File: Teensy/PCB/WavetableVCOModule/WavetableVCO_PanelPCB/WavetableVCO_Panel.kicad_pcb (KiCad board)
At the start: 2 copper layers, 61 x 128 mm, 15 parts, among them SW1 Next_File_Button

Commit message: Generated Gerbers
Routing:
- added copper zone on B.Cu, net extra
- added copper zone on F.Cu, net extra
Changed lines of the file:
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@@
       (layerselection 0x00010fc_ffffffff)
       (disableapertmacros false)
-      (usegerberextensions false)
-      (usegerberattributes true)
-      (usegerberadvancedattributes true)
-      (creategerberjobfile true)
+      (usegerberextensions true)
+      (usegerberattributes false)
+      (usegerberadvancedattributes false)
+      (creategerberjobfile false)
       (svguseinch false)
       (svgprecision 6)
@@
       (psa4output false)
       (plotreference true)
-      (plotvalue true)
+      (plotvalue false)
       (plotinvisibletext false)
       (sketchpadsonfab false)
-      (subtractmaskfromsilk false)
+      (subtractmaskfromsilk true)
       (outputformat 1)
       (mirror false)
-      (drillshape 1)
+      (drillshape 0)
       (scaleselection 1)
-      (outputdirectory "")
+      (outputdirectory "WavetableVCO_Panel_Gerber/")
     )
   )
   (net 0 "")
+  (net 1 "extra")
   (footprint "Perfboard:3.5mm Jack Perfboard_Hole" (layer "F.Cu")
     (at 129.54 154.1)
@@
       (effects (font (size 1 1) (thickness 0.15)))
     )
+    (fp_line (start -2.54 -64) (end 2.54 -64) (layer "User.1") (width 0.12))
     (fp_line (start -2.54 64) (end 2.54 64) (layer "User.1") (width 0.12))
-    (fp_line (start -2.54 -64) (end 2.54 -64) (layer "User.1") (width 0.12))
     (fp_circle (center 0 0) (end 0 0) (layer "User.1") (width 0.12) (fill none))
-    (fp_line (start -1.27 59.65) (end 1.27 59.65) (layer "User.2") (width 0.12))
-    (fp_line (start -1.27 62.85) (end 1.27 62.85) (layer "User.2") (width 0.12))
-    (fp_line (start -1.27 -62.85) (end 1.27 -62.85) (layer "User.2") (width 0.12))
-    (fp_line (start -1.27 -59.65) (end 1.27 -59.65) (layer "User.2") (width 0.12))
-    (fp_arc (start -1.27 62.85) (mid -2.87 61.25) (end -1.27 59.65) (layer "User.2") (width 0.12))
-    (fp_arc (start 1.27 59.65) (mid 2.87 61.25) (end 1.27 62.85) (layer "User.2") (width 0.12))
-    (fp_arc (start -1.27 -59.65) (mid -2.87 -61.25) (end -1.27 -62.85) (layer "User.2") (width 0.12))
-    (fp_arc (start 1.27 -62.85) (mid 2.87 -61.25) (end 1.27 -59.65) (layer "User.2") (width 0.12))
-    (pad "" np_thru_hole oval (at 0 -61.25) (size 5.74 3.2) (drill oval 5.74 3.2) (layers *.Mask))
-    (pad "" np_thru_hole oval (at 0 61.25) (size 5.74 3.2) (drill oval 5.74 3.2) (layers *.Mask))
+    (fp_line (start -1.6 59.65) (end 1.6 59.65) (layer "User.2") (width 0.12))
+    (fp_line (start -1.6 -59.65) (end 1.6 -59.65) (layer "User.2") (width 0.12))
+    (fp_line (start -1.6 62.85) (end 1.6 62.85) (layer "User.2") (width 0.12))
+    (fp_line (start -1.6 -62.85) (end 1.6 -62.85) (layer "User.2") (width 0.12))
+    (fp_arc (start 1.6 59.65) (mid 3.2 61.25) (end 1.6 62.85) (layer "User.2") (width 0.12))
+    (fp_arc (start 1.6 -62.85) (mid 3.2 -61.25) (end 1.6 -59.65) (layer "User.2") (width 0.12))
+    (fp_arc (start -1.6 -59.65) (mid -3.2 -61.25) (end -1.6 -62.85) (layer "User.2") (width 0.12))
+    (fp_arc (start -1.6 62.85) (mid -3.2 61.25) (end -1.6 59.65) (layer "User.2") (width 0.12))
+    (pad "1" thru_hole oval (at 0 -61.25) (size 7.4 4.2) (drill oval 6.4 3.2) (layers *.Cu *.Mask)
+      (net 1 "extra"))
+    (pad "1" thru_hole oval (at 0 61.25) (size 7.4 4.2) (drill oval 6.4 3.2) (layers *.Cu *.Mask)
+      (net 1 "extra"))
   )
   (footprint "Potentiometer:Bourns_PTV09A-XF_Hole" (layer "F.Cu")
@@
     (fp_line (start -2.54 -64) (end 2.54 -64) (layer "User.1") (width 0.12))
     (fp_circle (center 0 0) (end 0 0) (layer "User.1") (width 0.12) (fill none))
-    (fp_line (start -1.27 -59.65) (end 1.27 -59.65) (layer "User.2") (width 0.12))
-    (fp_line (start -1.27 62.85) (end 1.27 62.85) (layer "User.2") (width 0.12))
-    (fp_line (start -1.27 59.65) (end 1.27 59.65) (layer "User.2") (width 0.12))
-    (fp_line (start -1.27 -62.85) (end 1.27 -62.85) (layer "User.2") (width 0.12))
-    (fp_arc (start -1.27 -59.65) (mid -2.87 -61.25) (end -1.27 -62.85) (layer "User.2") (width 0.12))
-    (fp_arc (start -1.27 62.85) (mid -2.87 61.25) (end -1.27 59.65) (layer "User.2") (width 0.12))
-    (fp_arc (start 1.27 -62.85) (mid 2.87 -61.25) (end 1.27 -59.65) (layer "User.2") (width 0.12))
-    (fp_arc (start 1.27 59.65) (mid 2.87 61.25) (end 1.27 62.85) (layer "User.2") (width 0.12))
-    (pad "" np_thru_hole oval (at 0 61.25) (size 5.74 3.2) (drill oval 5.74 3.2) (layers *.Mask))
-    (pad "" np_thru_hole oval (at 0 -61.25) (size 5.74 3.2) (drill oval 5.74 3.2) (layers *.Mask))
+    (fp_line (start -1.6 62.85) (end 1.6 62.85) (layer "User.2") (width 0.12))
+    (fp_line (start -1.6 -62.85) (end 1.6 -62.85) (layer "User.2") (width 0.12))
+    (fp_line (start -1.6 59.65) (end 1.6 59.65) (layer "User.2") (width 0.12))
+    (fp_line (start -1.6 -59.65) (end 1.6 -59.65) (layer "User.2") (width 0.12))
+    (fp_arc (start -1.6 62.85) (mid -3.2 61.25) (end -1.6 59.65) (layer "User.2") (width 0.12))
+    (fp_arc (start 1.6 59.65) (mid 3.2 61.25) (end 1.6 62.85) (layer "User.2") (width 0.12))
+    (fp_arc (start -1.6 -59.65) (mid -3.2 -61.25) (end -1.6 -62.85) (layer "User.2") (width 0.12))
+    (fp_arc (start 1.6 -62.85) (mid 3.2 -61.25) (end 1.6 -59.65) (layer "User.2") (width 0.12))
+    (pad "1" thru_hole oval (at 0 61.25) (size 7.4 4.2) (drill oval 6.4 3.2) (layers *.Cu *.Mask)
+      (net 1 "extra"))
+    (pad "1" thru_hole oval (at 0 -61.25) (size 7.4 4.2) (drill oval 6.4 3.2) (layers *.Cu *.Mask)
+      (net 1 "extra"))
   )
   (footprint "Perfboard:3.5mm Jack Perfboard_Hole" (layer "F.Cu")
@@
   (gr_rect (start 91.442322 56.66449) (end 126.999967 82.065685) (layer "Edge.Cuts") (width 0.05) (fill none))
   (gr_rect (start 78.74 45.72) (end 139.7 173.72) (layer "Edge.Cuts") (width 0.05) (fill none))
+  (zone (net 1) (net_name "extra") (layers F&B.Cu) (hatch edge 0.508)
+    (connect_pads yes (clearance 0.508))
+    (min_thickness 0.254) (filled_areas_thickness no)
+    (fill yes (thermal_gap 0.508) (thermal_bridge_width 0.508))
+    (polygon
+      (pts
+        (xy 139.7 173.736)
+        (xy 78.74 173.736)
+        (xy 78.74 45.72)
+        (xy 139.7 45.72)
+      )
+    )
+  )
 )

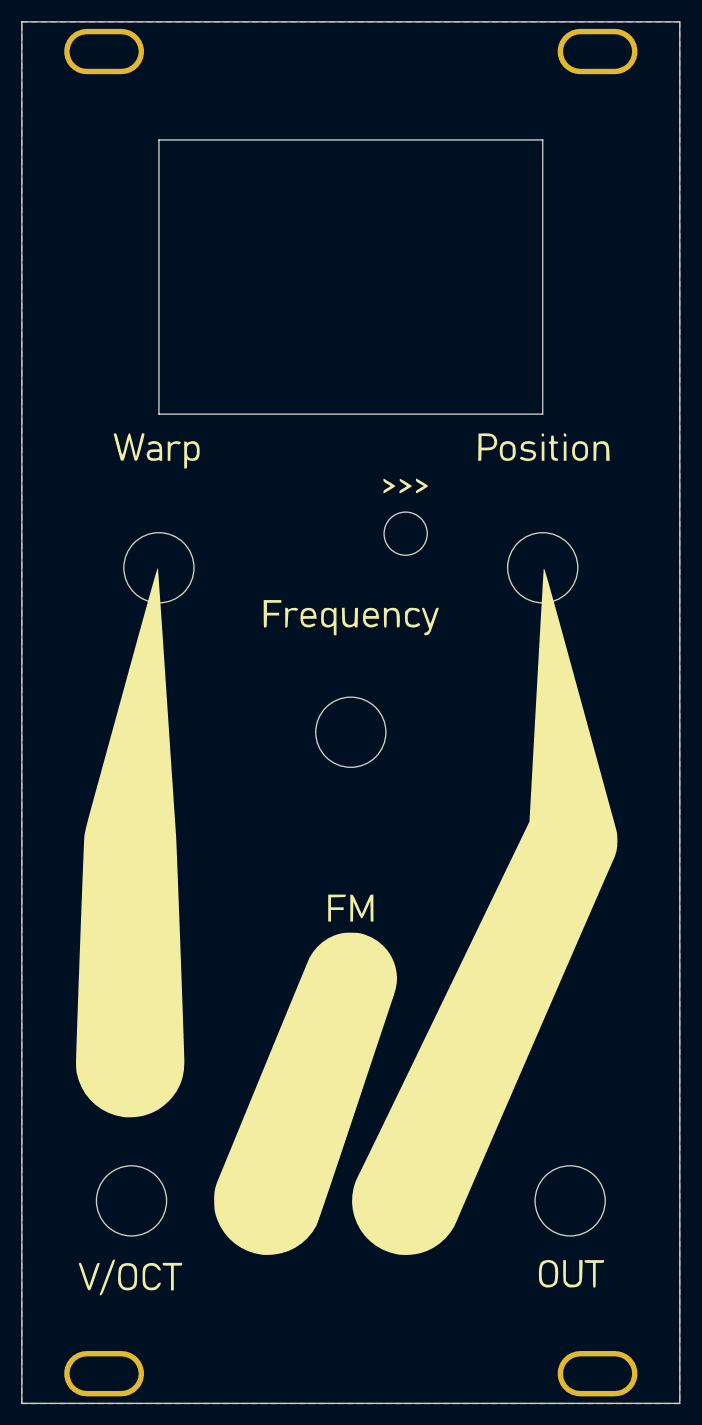
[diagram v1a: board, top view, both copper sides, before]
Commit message: Added USB-C Power Supply
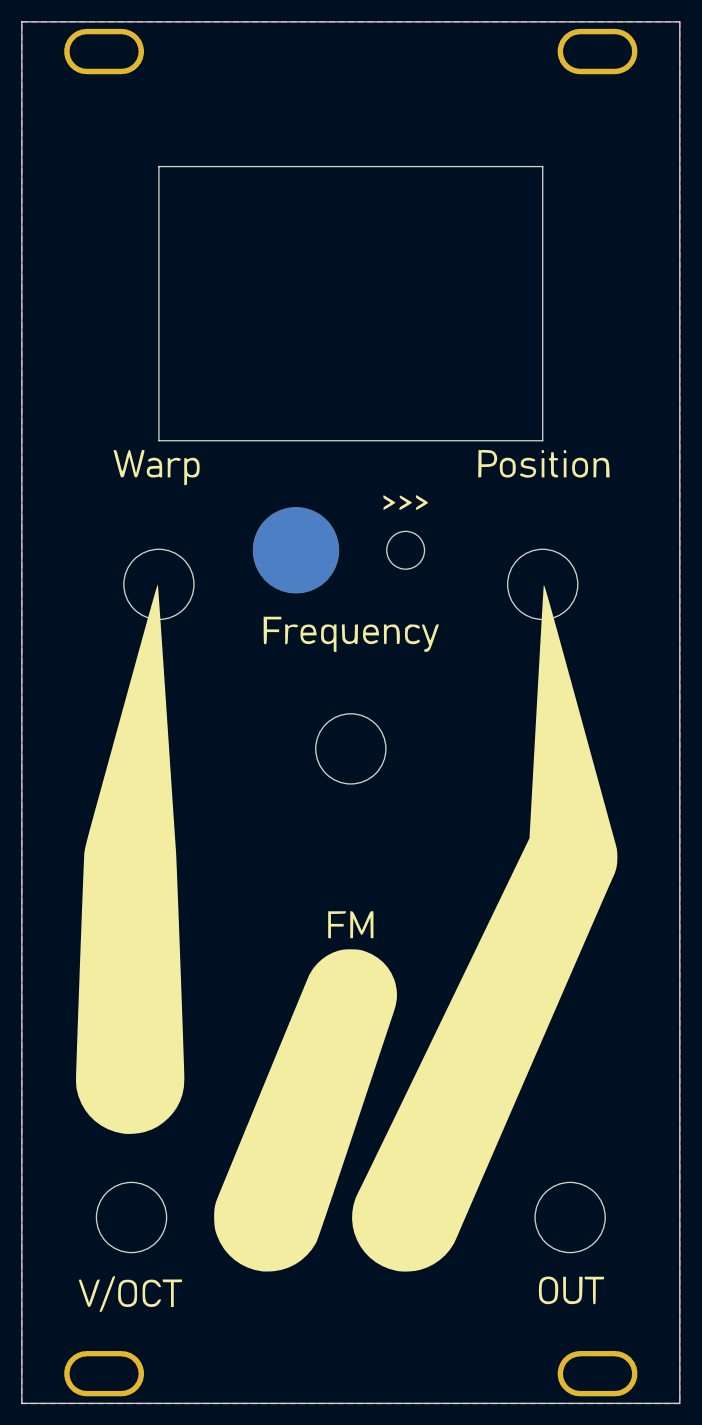
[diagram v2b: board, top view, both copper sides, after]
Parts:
- added REF**: Würth_REDCUBE_SMD_7466203, Misc:Würth_REDCUBE_SMD_7466203, B.Cu at (104.1, 94.7)
- moved G*** 1.54 mm to (109.2, 112.3)
- moved RV1 1.54 mm to (91.4, 104.8)
- moved RV5 1.54 mm to (127.0, 104.8)
- moved SW1 1.54 mm to (111.0, 92.4)
- moved IJ1 1.54 mm to (88.9, 142.9)
- moved IJ2 1.54 mm to (88.9, 155.6)
- moved IJ3 1.54 mm to (101.6, 155.6)
- moved IJ4 1.54 mm to (114.3, 155.6)
- moved OJ1 1.54 mm to (129.5, 155.6)
- moved RV2 1.54 mm to (88.8, 130.2)
- moved RV3 1.54 mm to (109.2, 120.1)
- moved RV4 1.54 mm to (109.2, 142.9)
- moved RV6 1.54 mm to (129.5, 130.2)
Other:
- outline, holes or cut-outs redrawn
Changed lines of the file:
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@@
   )
   (setup
+    (stackup
+      (layer "F.SilkS" (type "Top Silk Screen") (color "White"))
+      (layer "F.Paste" (type "Top Solder Paste"))
+      (layer "F.Mask" (type "Top Solder Mask") (color "Black") (thickness 0.01))
+      (layer "F.Cu" (type "copper") (thickness 0.035))
+      (layer "dielectric 1" (type "core") (thickness 1.51) (material "FR4") (epsilon_r 4.5) (loss_tangent 0.02))
+      (layer "B.Cu" (type "copper") (thickness 0.035))
+      (layer "B.Mask" (type "Bottom Solder Mask") (color "Black") (thickness 0.01))
+      (layer "B.Paste" (type "Bottom Solder Paste"))
+      (layer "B.SilkS" (type "Bottom Silk Screen") (color "White"))
+      (copper_finish "ENIG")
+      (dielectric_constraints no)
+    )
     (pad_to_mask_clearance 0)
     (pcbplotparams
@@
   (net 1 "extra")
   (footprint "Perfboard:3.5mm Jack Perfboard_Hole" (layer "F.Cu")
-    (at 129.54 154.1)
+    (at 129.54 155.64)
     (property "Sheetfile" "../Subcircuits/Output/Output.kicad_sch")
     (property "Sheetname" "Channel_1_Mod_Output")
@@
       (effects (font (size 1 1) (thickness 0.15)))
     )
-    (fp_text value "Screw_Slots" (at 0 5.08 unlocked) (layer "F.Fab")
-      (effects (font (size 1 1) (thickness 0.15)))
-    )
-    (fp_text user "${REFERENCE}" (at 0 6.58 unlocked) (layer "F.Fab")
+    (fp_text value "Screw_Slots" (at 0 6.62 unlocked) (layer "F.Fab")
+      (effects (font (size 1 1) (thickness 0.15)))
+    )
+    (fp_text user "${REFERENCE}" (at 0 8.12 unlocked) (layer "F.Fab")
       (effects (font (size 1 1) (thickness 0.15)))
     )
@@
   )
   (footprint "Potentiometer:Bourns_PTV09A-XF_Hole" (layer "F.Cu")
-    (at 91.44 103.3)
+    (at 91.44 104.84)
     (descr "Bourns_PTV09A-4025FB103, http://www.bourns.com/docs/Product-Datasheets/ptv09.pdf")
     (tags "Potentiometer vertical Bourns PTV09A-1 Single")
@@
       (effects (font (size 1 1) (thickness 0.15)))
     )
-    (fp_text user "${REFERENCE}" (at 0 -1.985 -180) (layer "F.Fab")
+    (fp_text user "${REFERENCE}" (at 0 -1.985) (layer "F.Fab")
       (effects (font (size 1 1) (thickness 0.15)))
     )
@@
   )
   (footprint "Potentiometer:Bourns_PTV09A-X_Hole" (layer "F.Cu")
-    (at 109.22 141.4)
+    (at 109.22 142.94)
     (descr "Bourns_PTV09A-4025FB103, http://www.bourns.com/docs/Product-Datasheets/ptv09.pdf")
     (tags "Potentiometer vertical Bourns PTV09A-1 Single")
@@
       (effects (font (size 1 1) (thickness 0.15)))
     )
-    (fp_text user "${REFERENCE}" (at 0 -1.985 -180) (layer "F.Fab")
+    (fp_text user "${REFERENCE}" (at 0 -1.985) (layer "F.Fab")
       (effects (font (size 1 1) (thickness 0.15)))
     )
@@
   )
   (footprint "Potentiometer:Bourns_PTV09A-X_Hole" (layer "F.Cu")
-    (at 129.495 128.685)
+    (at 129.495 130.225)
     (descr "Bourns_PTV09A-4025FB103, http://www.bourns.com/docs/Product-Datasheets/ptv09.pdf")
     (tags "Potentiometer vertical Bourns PTV09A-1 Single")
@@
       (effects (font (size 1 1) (thickness 0.15)))
     )
-    (fp_text user "${REFERENCE}" (at 0 -1.985 -180) (layer "F.Fab")
+    (fp_text user "${REFERENCE}" (at 0 -1.985) (layer "F.Fab")
       (effects (font (size 1 1) (thickness 0.15)))
     )
@@
       (effects (font (size 1 1) (thickness 0.15)))
     )
-    (fp_text value "Screw_Slots" (at 0 5.08 unlocked) (layer "F.Fab")
-      (effects (font (size 1 1) (thickness 0.15)))
-    )
-    (fp_text user "${REFERENCE}" (at 0 6.58 unlocked) (layer "F.Fab")
+    (fp_text value "Screw_Slots" (at 0 6.62 unlocked) (layer "F.Fab")
+      (effects (font (size 1 1) (thickness 0.15)))
+    )
+    (fp_text user "${REFERENCE}" (at 0 8.12 unlocked) (layer "F.Fab")
       (effects (font (size 1 1) (thickness 0.15)))
     )
@@
   )
   (footprint "Perfboard:3.5mm Jack Perfboard_Hole" (layer "F.Cu")
-    (at 114.3 154.1)
+    (at 114.3 155.64)
     (property "Sheetfile" "../Subcircuits/Input/Input.kicad_sch")
     (property "Sheetname" "Position_Mod_Input")
@@
   )
   (footprint "Potentiometer:Bourns_PTV09A-XF_Hole" (layer "F.Cu")
-    (at 109.22 118.54)
+    (at 109.22 120.08)
     (descr "Bourns_PTV09A-4025FB103, http://www.bourns.com/docs/Product-Datasheets/ptv09.pdf")
     (tags "Potentiometer vertical Bourns PTV09A-1 Single")
@@
       (effects (font (size 1 1) (thickness 0.15)))
     )
-    (fp_text user "${REFERENCE}" (at 0 -1.985 -180) (layer "F.Fab")
+    (fp_text user "${REFERENCE}" (at 0 -1.985) (layer "F.Fab")
       (effects (font (size 1 1) (thickness 0.15)))
     )
@@
   )
   (footprint "Potentiometer:Bourns_PTV09A-X_Hole" (layer "F.Cu")
-    (at 88.815 128.685)
+    (at 88.815 130.225)
     (descr "Bourns_PTV09A-4025FB103, http://www.bourns.com/docs/Product-Datasheets/ptv09.pdf")
     (tags "Potentiometer vertical Bourns PTV09A-1 Single")
@@
       (effects (font (size 1 1) (thickness 0.15)))
     )
-    (fp_text user "${REFERENCE}" (at 0 -1.985 -180) (layer "F.Fab")
+    (fp_text user "${REFERENCE}" (at 0 -1.985) (layer "F.Fab")
       (effects (font (size 1 1) (thickness 0.15)))
     )
@@
   )
   (footprint "LOGO" (layer "F.Cu")
-    (at 109.22 110.72)
+    (at 109.22 112.26)
     (attr board_only exclude_from_pos_files exclude_from_bom)
     (fp_text reference "G***" (at 0 0) (layer "F.SilkS") hide
@@
   )
   (footprint "Perfboard:3.5mm Jack Perfboard_Hole" (layer "F.Cu")
-    (at 88.9 141.4)
+    (at 88.9 142.94)
     (property "Sheetfile" "../Subcircuits/Input/Input.kicad_sch")
     (property "Sheetname" "Warp_Mod_Input")
@@
   )
   (footprint "Perfboard:3.5mm Jack Perfboard_Hole" (layer "F.Cu")
-    (at 101.6 154.1)
+    (at 101.6 155.64)
     (property "Sheetfile" "../Subcircuits/Input/Input.kicad_sch")
     (property "Sheetname" "FM_Mod_Input")
@@
   )
   (footprint "Perfboard:3.5mm Jack Perfboard_Hole" (layer "F.Cu")
-    (at 88.9 154.1)
+    (at 88.9 155.64)
     (property "Sheetfile" "../Subcircuits/Input/Input.kicad_sch")
     (property "Sheetname" "VOCT_Input")
@@
   )
   (footprint "Button_Switch_THT:SW_PUSH_6mm_H13mm" (layer "F.Cu")
-    (at 111.05 90.89)
+    (at 111.05 92.43)
     (descr "tactile push button, 6x6mm e.g. PHAP33xx series, height=13mm")
     (tags "tact sw push 6mm")
@@
       (effects (font (size 1 1) (thickness 0.15)))
     )
-    (pad "" np_thru_hole circle (at 3.25 2.25) (size 4 4) (drill 4) (layers *.Mask))
+    (pad "" np_thru_hole circle (at 3.25 2.25) (size 3.5 3.5) (drill 3.5) (layers *.Mask))
     (model "${KICAD6_3DMODEL_DIR}/Button_Switch_THT.3dshapes/SW_PUSH_6mm_H13mm.wrl" hide
       (offset (xyz 0 0 0))
@@
   )
   (footprint "Potentiometer:Bourns_PTV09A-XF_Hole" (layer "F.Cu")
-    (at 127 103.3)
+    (at 127 104.84)
     (descr "Bourns_PTV09A-4025FB103, http://www.bourns.com/docs/Product-Datasheets/ptv09.pdf")
     (tags "Potentiometer vertical Bourns PTV09A-1 Single")
@@
       (effects (font (size 1 1) (thickness 0.15)))
     )
-    (fp_text user "${REFERENCE}" (at 0 -1.985 -180) (layer "F.Fab")
+    (fp_text user "${REFERENCE}" (at 0 -1.985) (layer "F.Fab")
       (effects (font (size 1 1) (thickness 0.15)))
     )
@@
     )
   )
-  (gr_rect (start 91.442322 56.66449) (end 126.999967 82.065685) (layer "Edge.Cuts") (width 0.05) (fill none))
+  (footprint "Misc:Würth_REDCUBE_SMD_7466203" (layer "B.Cu")
+    (at 104.14 94.68 180)
+    (attr smd)
+    (fp_text reference "REF**" (at 0 -7.62 unlocked) (layer "B.SilkS") hide
+      (effects (font (size 1 1) (thickness 0.15)) (justify mirror))
+    )
+    (fp_text value "Würth_REDCUBE_SMD_7466203" (at 0 -9.12 unlocked) (layer "B.Fab")
+      (effects (font (size 1 1) (thickness 0.15)) (justify mirror))
+    )
+    (fp_text user "${REFERENCE}" (at 0 -10.62 unlocked) (layer "B.Fab")
+      (effects (font (size 1 1) (thickness 0.15)) (justify mirror))
+    )
+    (pad "1" smd circle (at 0 0 180) (size 8 8) (layers "B.Cu" "B.Paste" "B.Mask")
+      (net 1 "extra") (zone_connect 1) (thermal_width 2) (thermal_gap 1))
+  )
+  (gr_rect (start 91.442322 59.12949) (end 126.999967 84.530685) (layer "Edge.Cuts") (width 0.05) (fill none))
   (gr_rect (start 78.74 45.72) (end 139.7 173.72) (layer "Edge.Cuts") (width 0.05) (fill none))
+  (gr_line (start 81.28 54.72) (end 81.28 164.72) (layer "User.3") (width 0.1))
   (zone (net 1) (net_name "extra") (layers F&B.Cu) (hatch edge 0.508)
     (connect_pads yes (clearance 0.508))
